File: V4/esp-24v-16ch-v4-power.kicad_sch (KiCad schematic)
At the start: 39 parts, among them J5 VIN, J6 USB_C_Receptacle_USB2.0, Q1 WPM2015-3/TR, Q2 MMUN2211LT3G, U1 SY8089A1AAC, U2 TX4138, U9 XC6206PxxxMR

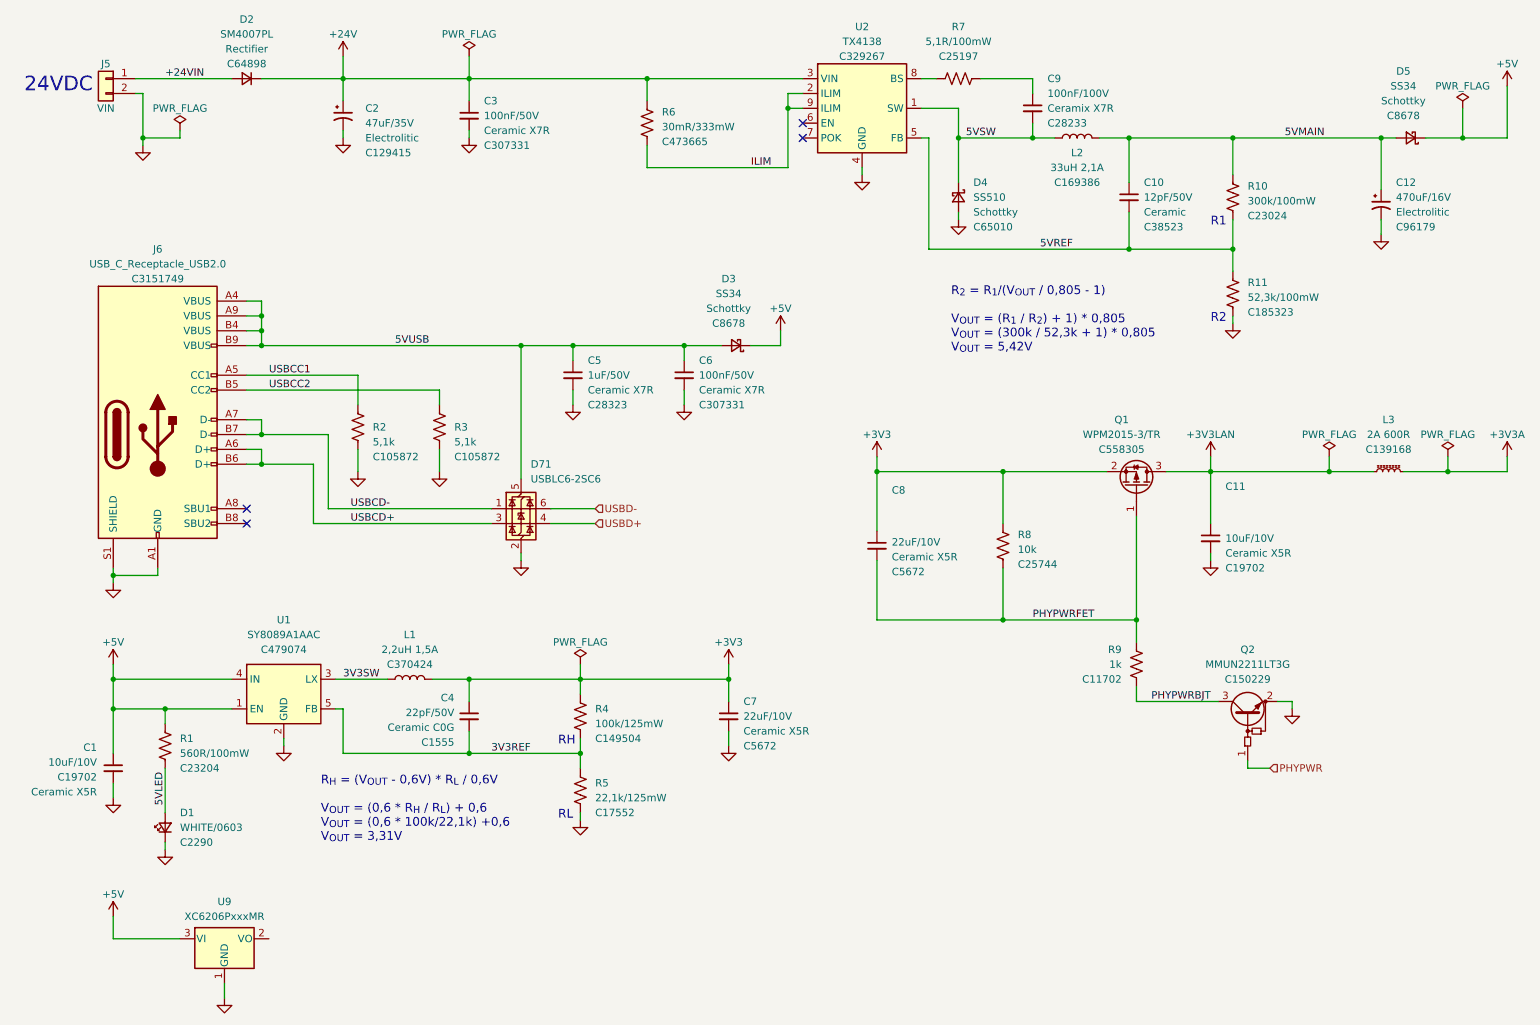
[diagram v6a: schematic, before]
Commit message: Rerouting
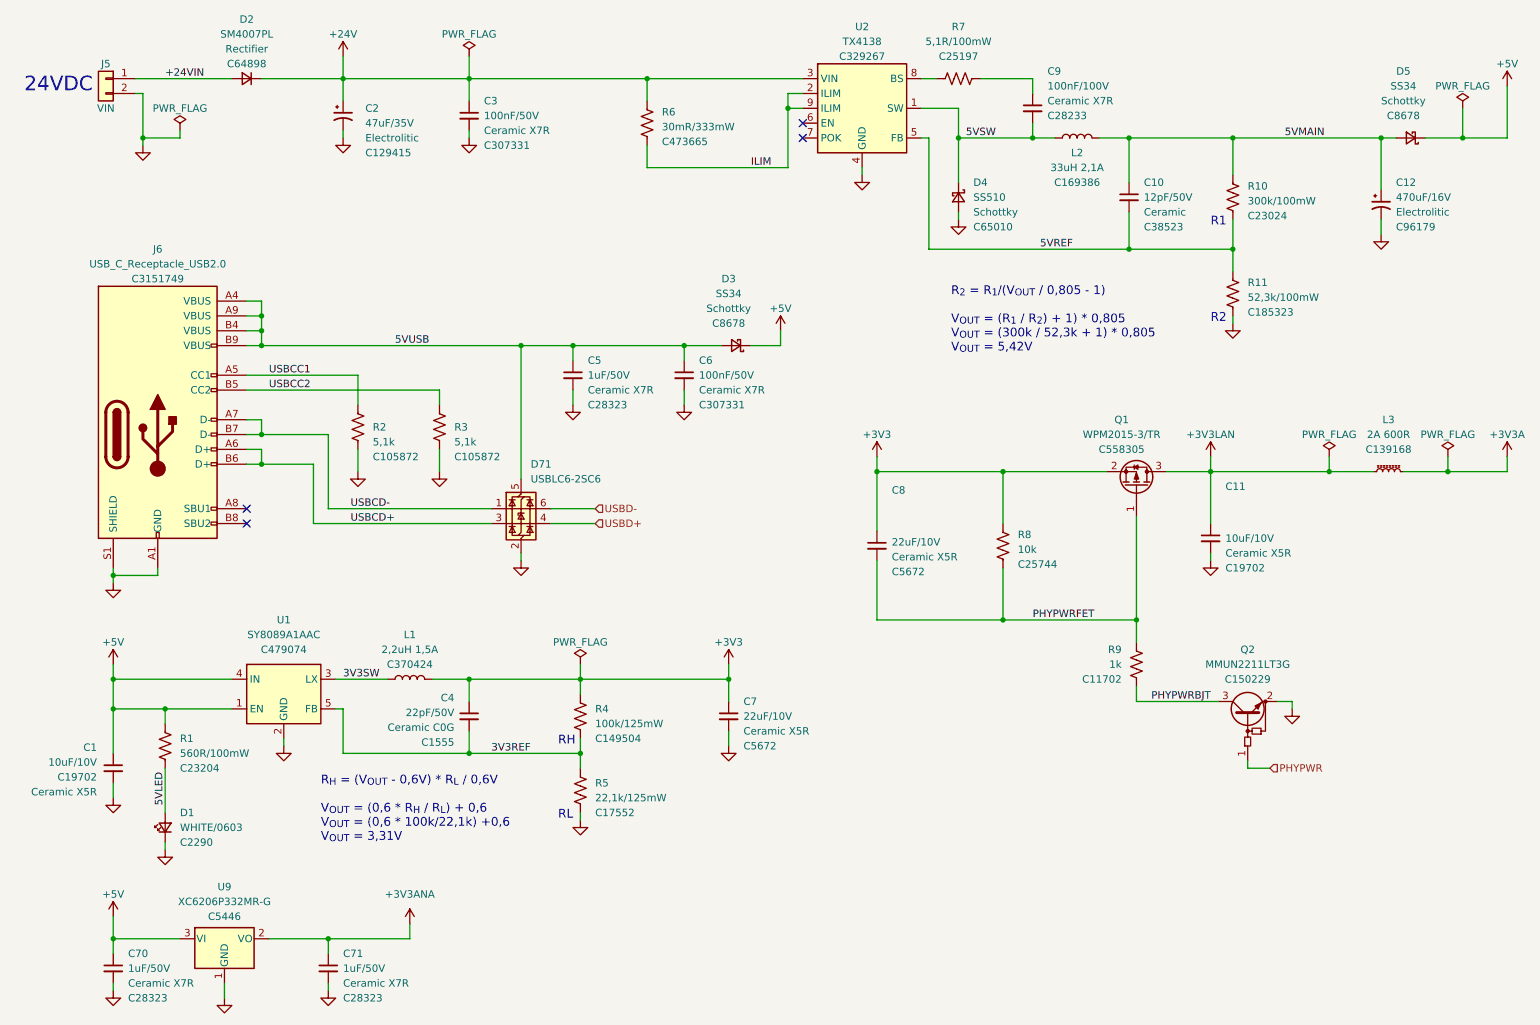
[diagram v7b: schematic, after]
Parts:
- added C70, C71: 1uF/50V, Tales:C_0805_2012Metric, symbol Device:C_Small
- C9: Technology Ceramix X7R -> Ceramic X7R
- U9: value XC6206PxxxMR -> XC6206P332MR-G; Case (none) -> SOT-23-3L; JLCPCB BOM (none) -> 1; LCSC Part # (none) -> C5446; Mfr (none) -> Torex Semicon; Mfr PN (none) -> XC6206P332MR-G; Vendor (none) -> JLCPCB; Vendor PN (none) -> C5446
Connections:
- net +5V: now also C70.1
- net GND: now also C70.2, C71.2
- net +3V3ANA: now reaches U9.2 (VO)
- net +3V3ANA: now also C71.1

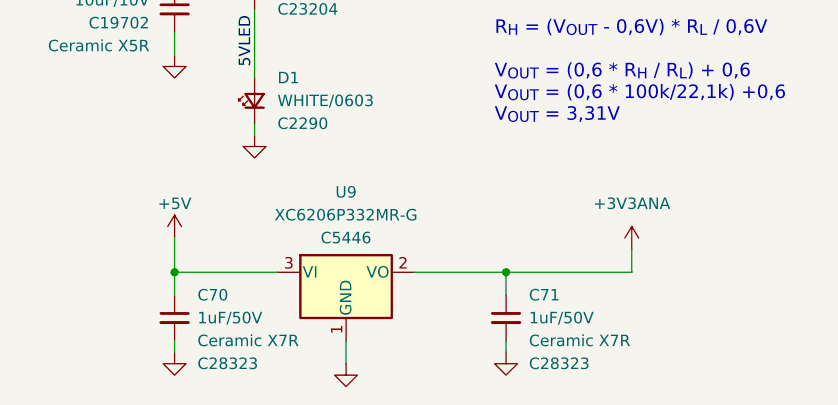
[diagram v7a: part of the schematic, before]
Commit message: Rerouting
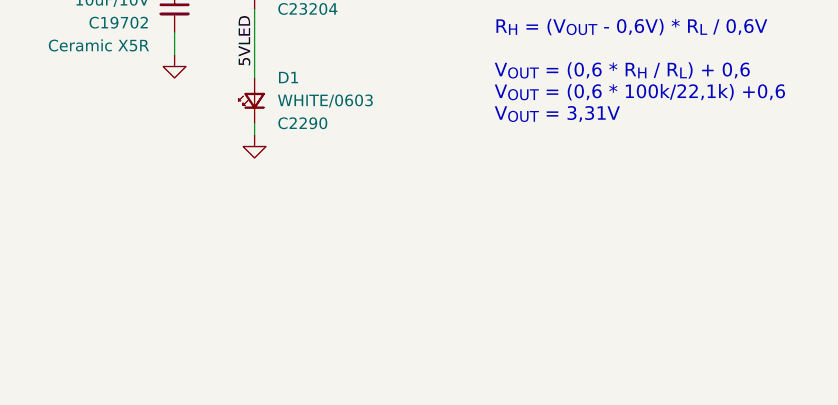
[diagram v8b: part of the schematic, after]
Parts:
- removed C70, C71: 1uF/50V, Tales:C_0805_2012Metric, symbol Device:C_Small
- removed U9: XC6206P332MR-G, Package_TO_SOT_SMD:SOT-23-3, symbol Regulator_Linear:XC6206PxxxMR
- D71: Case (none) -> SOT-23-6L; JLCPCB BOM (none) -> 1; LCSC Part # (none) -> C7519; Mfr (none) -> STMicroelectronics; Mfr PN (none) -> USBLC6-2SC6; Vendor (none) -> JLCPCB; Vendor PN (none) -> C7519
